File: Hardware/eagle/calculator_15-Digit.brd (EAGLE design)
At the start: 154.9 x 53.3 mm, 144 parts, among them M1 IRLML6402, M10 IRLML6401, M11 IRLML6401, M12 IRLML6402, M2 IRLML6402, M3 IRLML6401, M4 IRLML6401, M5 IRLML6401, M6 IRLML6401, M7 IRLML6401, M8 IRLML6401, M9 IRLML6401, U1 74HC4051_MUX, U2 TC1262-3.3VDB, U3 ATMEGA1284P-PU, U5 CON, X1 MICROMATCH-12, X3 MICROMATCH-12, Y2 12MHz

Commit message: New Hardware Design V0.4
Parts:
- removed BH1, BH2, BH3: BATTERY_HOLDER_AAAHOLDER_AAA, SparkFun-Electromechanical:BATTERY-AAA-KIT
- removed C12, C19: 15n, rcl:C025_050-025X075
- removed C17: 1n, rcl:C025_050-025X075
- removed C9: 2µ2, _jc:C025_050-025X075
- removed D29: SD103CW, BaseApp:SMADIODE
- removed JP3: DCF77, adafruit:1X01-CLEANBIG
- removed M12, M2: IRLML6402, IRLML6402:SOT-23
- removed R27, R45: 27k, rcl:0204/7
- removed R28: 6k8, rcl:0204/7
- removed R44: 47k, rcl:0204/7
- removed R46, R47, R53: 8k2, rcl:0204/7
- removed R52: 22, rcl:0204/7
- removed S2: RESET, _jc:B3F-10XX
- removed U2: TC1262-3.3VDB, parts:SOT223
- removed U5: CON, BaseApp:AUDIO-JACK
- added BH10, BH12, BH8: HOLDER_AAA_RIGHT, SparkFun-Electromechanical:BATTERY-AAA-RIGHT
- added BH11, BH7, BH9: HOLDER_AAA_LEFT1, SparkFun-Electromechanical:BATTERY-AAA-LEFT
- added C16: 0.1uF, SparkFun:0805
- added C20, C21: 10uF, SparkFun:EIA3216
- added C22: 15n, rcl:C1206K
- added D10, D7, D8, D9: SD103CW, BaseApp:SMADIODE
- added R2: 6k8, rcl:0204/5
- added R3: 27k, rcl:R1206
- added S3: B3F-4150, SmartPrj:TACTILE-PTH-12MM
- added U$1: IRLML6244, transistor-power:MICRO3
- added U4: TLV70033, SparkFun:SOT23-5
- C10: device rcl:C025_050-025X075 -> rcl:C1206K
- C11: value 15n -> 1n; device rcl:C025_050-025X075 -> SparkFun:0805
- C5: value 2µ2 -> 15n; device _jc:C025_050-025X075 -> rcl:C1206K
- JP13, JP14: value PINHD-2X7 -> (none); device pinhead:ZX07 -> pinhead:2X07
- M1: value IRLML6402 -> IRLML2244
- M10, M11, M3, M4, M5, M6, M7, M8, M9: value IRLML6401 -> IRLML2244
- R20: value 27k -> 2R7; device rcl:0204/7 -> rcl:0204/5
- R23: value 27k -> 6k8; device rcl:0204/7 -> rcl:R1206
- R24: value 6k8 -> 2R7; device rcl:0204/7 -> rcl:R1206
- R25: value 27k -> 100
- R26: value 6k8 -> 27k; device rcl:0204/7 -> rcl:0204/5
- R30: value 3k3 -> 3V3
- R31: value 68 -> 39
- R32: value 100 -> 39
- R35: value 8k2 -> 3k3
- R48: value 1k -> 3k3
- SG1: value BUZZERPTH-KIT -> BUZZERNS; device SparkFun-Electromechanical:BUZZER-12MM-KIT -> SparkFun-Electromechanical:BUZZER-12MM-NS
- U$2: value IRLML2502 -> IRLML6244
- moved C5 225.1 mm to (-68.6, -68.6), turned to 0 degrees
- moved R25 103.0 mm to (-66.0, -76.2)
- moved R23 85.3 mm to (-48.3, -45.7)
- moved R24 54.9 mm to (-48.3, -7.62)
- moved R20 42.1 mm to (-45.7, -15.2), turned to 0 degrees
- moved C10 40.5 mm to (-55.9, 15.2), turned to 180 degrees
- moved C11 40.3 mm to (-50.8, 15.2), turned to 180 degrees
- moved R26 35.3 mm to (-58.4, 7.62), turned to 180 degrees
- moved D6 34.5 mm to (-58.4, -48.3), turned to 180 degrees
- moved D1 24.0 mm to (-58.4, -55.9), turned to 180 degrees
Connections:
- net D11 renamed D5_
- net D12 renamed D6_
- net D13 renamed D7_
- net D14 renamed D0_
- net RXD_0 renamed D8_
- net TXD_0 renamed D9_
- removed net 3V5: C1.1, C2.1, C3.1, C6.1, D5.C, D6.C, JP5.2, R1.1, R21.1, R22.1, R4.1, U2.3, U3.10
- removed net A_0: KP1.C_2, KP2.C_2, R24.1
- removed net A_1: KP1.C_1, KP2.C_1, R26.1
- removed net A_2: KP1.C_0, KP2.C_0, R28.1
- removed net D4: C17.1, R35.1, U3.18
- removed net INH: R45.1, U$2.3, U1.6
- removed net N$24: C15.1, R31.1, R32.2
- removed net N$29: M3.1, R34.1, R48.2
- removed net N$8: C19.1, M12.1, M2.1, R45.2, R47.1
- removed net N$9: R46.1, R47.2, S2.1, S2.2
- removed net OFF: D29.A, R20.2, R44.1, U$2.1
- removed net SEG_C_SOURCE: JP10.1, M6.3
- removed net SEG_DP_SOURCE: JP7.1, M11.3
- removed net V_DCF77: C9.1, R52.2, R53.1, U5.TIP
- new net 3V3: C1.1, C16.1, C2.1, C20.A, C3.1, C6.1, D5.C, D6.C, D7.A, R1.1, R21.1, R22.1, R4.1, U3.10, U4.5
- new net A8: C22.1, R35.1, R48.2
- new net A9: C5.1, R25.1, R26.2, R3.2
- new net D12_: D9.A, D9.C, R48.1, U$1.2, U$1.3, U3.18
- new net EN: C10.1, C5.2, D10.C, R2.2, R23.2, R26.1, R3.1, U$2.1, U4.3
- new net GND1: C22.2
- new net IO: U$2.3, U1.3
- new net N$6: S3.P$13, S3.P$14, S3.P$23, S3.P$24, S3.P$3, S3.P$4
- new net XX4: C14.2, C15.2, R32.1, SG1.-
- new net XX_3: D8.A, R20.1, R24.1
- net A0: now also C15.1, R31.1; no longer R32.1
- net A4: now also R32.2
- net A5: now also KP1.C_0, KP2.C_0; no longer C12.1, R27.1, R28.2
- net A6: now also KP1.C_1, KP2.C_1; no longer C11.1, R25.1, R26.2
- net A7: now also KP1.C_2, KP2.C_2; no longer C10.1, R23.1, R24.2
- net AREF: no longer C5.1, R23.2, R25.2, R27.2
- net D18: now also D10.A, U$1.1; no longer D29.C
- net D7: no longer JP3.1, JP6.2, R53.2, U5.RING
- net GND: now also C16.2, C20.C, C21.C, JP6.2, R2.1, R23.1, S3.P$15, U1.6, U4.2; no longer BH1.M1, BH1.M2, C12.2, C14.2, C15.2, C5.2, C9.2, SG1.-, U1.3, U5.SLEEVE
- net GND_POWER: no longer R20.1, S2.3, S2.4, U$2.2, U2.2, U2.4
- net N$1: now also M3.1, R34.1; no longer C17.2, R48.1
- net N$2: now also U$2.2; no longer BH1.P1, BH1.P2, BH2.M1, BH2.M2
- net N$3: now also C11.1, U4.4; no longer BH2.P1, BH2.P2, BH3.M1, BH3.M2
- net N$7: now also D8.C; no longer M12.2, M2.2, R46.2
- net NC1: now also BH11.P1, BH11.P2, BH11.P3, BH11.P4, BH4.P3, BH4.P4, BH7.P1, BH7.P2, BH7.P3, BH7.P4, BH9.P1, BH9.P2, BH9.P3, BH9.P4
- net NC2: now also BH5.P3, BH5.P4
- net NC3: now also BH10.M1, BH10.M2, BH10.M3, BH10.M4, BH12.M1, BH12.M2, BH12.M3, BH12.M4, BH6.M3, BH6.M4, BH8.M1, BH8.M2, BH8.M3, BH8.M4
- net SEG_C: now also JP10.1, M6.3
- net SEG_DP: now also JP7.1, M11.3
- net VCC: now also JP5.2, R20.2, R24.2; no longer BH3.P1, BH3.P2, M2.3
- net V_IN: now also C21.A, D7.C, S3.P$1, S3.P$11, S3.P$12, S3.P$2, S3.P$21, S3.P$22, U4.1; no longer C19.2, M12.3, R44.2, R52.1, U2.1
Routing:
- net SEG_DP: track 327.7 -> 347.3 mm
- net SEG_DP_SOURCE: track 19.6 -> 0.00 mm
- net SEG_C_SOURCE: track 9.56 -> 0.00 mm
- net SEG_C: track 271.7 -> 281.2 mm

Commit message: New Hardware Design V0.4a
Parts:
- removed C13: 15n, rcl:C025_050-025X075
- removed D10, D9: SD103CW, BaseApp:SMADIODE
- removed S1: RESET, _jc:B3F-10XX
- removed U$1: IRLML6244, transistor-power:MICRO3
- removed X2, X4: (no value), pinhead:2X06
- added C12: 0.1uF, SparkFun:0805
- added C9: 1µ, rcl:C025_050-025X075
- added D11, D12: SD103CW, BaseApp:SMADIODE
- added M2: IRLML2244, IRLML6402:SOT-23
- added R27: 6k8, rcl:R1206
- added R28, R44: 47k, rcl:0204/7
- C18: value 15n -> 100n
- C4: value 2µ2 -> 1µ; device _jc:C025_050-025X075 -> rcl:C025_050-025X075
- R1: value 68k -> 47k
- R26, R3: value 27k -> 6k8
- R31, R32: value 39 -> 100
- moved C5 94.4 mm to (-30.5, 17.8)
- moved R25 94.4 mm to (-27.9, 10.2)
- moved C4 55.7 mm to (-30.5, 5.08)
- moved U3 50.6 mm to (53.3, 1.27), turned to 270 degrees
- moved C10 40.2 mm to (-33.0, -17.8), turned to 0 degrees
- moved D8 36.6 mm to (-66.0, -30.5)
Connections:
- net D8 renamed D2_
- net SCL renamed D16_
- net SDA renamed D17_
- removed net 3V3: C1.1, C16.1, C2.1, C20.A, C3.1, C6.1, D5.C, D6.C, D7.A, R1.1, R21.1, R22.1, R4.1, U3.10, U4.5
- removed net D10: JP13.9, U3.5, X2.7
- removed net D15: U3.2
- removed net D18: D10.A, U$1.1, U3.24
- removed net D19: JP14.7, U3.25, X4.7
- removed net D2: JP1.1, U3.16
- removed net D20: JP14.6, U3.26, X4.6
- removed net D21: JP14.5, U3.27, X4.5
- removed net D22: JP14.4, U3.28, X4.4
- removed net D23: JP14.3, U3.29, X4.3
- removed net D3: JP2.1, U3.17
- removed net D5: JP13.8, U3.19, X2.6
- removed net D6: JP13.7, U3.20, X2.5
- removed net D7: U3.21
- removed net D9: U3.4
- removed net IO: U$2.3, U1.3
- removed net IO_A__: JP13.11, X2.9
- removed net IO_B__: JP13.12, X2.10
- removed net IO_C__: JP13.13, X2.11
- removed net IO_D__: JP13.14, X2.12
- removed net N$7: D8.C
- removed net XX4: C14.2, C15.2, R32.1, SG1.-
- new net CA_PWM1: D12.A, M2.3
- new net D10_: JP1.1, JP13.10, U3.16
- new net D11_: JP13.8, JP2.1, U3.17
- new net D13_: JP13.7, U3.19
- new net D14_: JP14.1, U3.20
- new net D15_: JP14.2, U3.21
- new net D18_: R44.2, U3.24
- new net D19_: JP14.3, U3.25
- new net D1_: JP13.14, U3.2
- new net D20_: JP14.4, U3.26
- new net D21_: JP14.5, U3.27
- new net D22_: JP14.6, U3.28
- new net D23_: JP14.7, U3.29
- new net D3_: JP13.11, U3.4
- new net D4_: U3.5
- new net EN_: D11.C, D12.C, R27.1
- new net GND-ISO: C1.2, C12.2, C14.2, C15.2, C2.2, C3.2, C4.2, C6.2, C7.2, C8.2, D4.C, D5.A, JP5.6, JP6.1, JP6.2, U$2.3, U1.3, U1.6, U1.7, U1.8, U3.11, U3.31
- new net N$10: C15.1, C9.2, R32.1, SG1.-
- new net N$8: M2.1, R28.2, R44.1
- net /RESET: no longer S1.1, S1.2
- net A0: no longer C15.1
- net A5: now also KP1.C_2, KP2.C_2; no longer KP1.C_0, KP2.C_0
- net A7: now also KP1.C_0, KP2.C_0; no longer KP1.C_2, KP2.C_2
- net AREF: now also C12.1; no longer C13.1
- net CA_PWM: no longer X4.8
- net D0_: now also JP13.13
- net D12_: no longer D9.A, D9.C, U$1.2, U$1.3
- net D5_: no longer JP13.10, X2.8
- net D6_: now also JP13.12; no longer JP14.1, X4.1
- net D7_: now also JP13.9; no longer JP14.2, X4.2
- net EN: now also R27.2; no longer D10.C
- net GND: no longer C1.2, C13.2, C2.2, C3.2, C4.2, C6.2, C7.2, C8.2, D4.C, D5.A, JP5.6, JP6.1, JP6.2, S1.3, S1.4, U1.6, U1.7, U1.8, U3.11, U3.31
- net IO_A: no longer X2.4
- net IO_B: no longer X2.3
- net IO_C: no longer X2.2
- net IO_D: no longer X2.1
- net IO_DP: no longer X4.9
- net IO_E: no longer X4.12
- net IO_F: no longer X4.11
- net IO_G: no longer X4.10
- net N$23: now also C9.1
- net VCC: now also C1.1, C16.1, C2.1, C20.A, C3.1, C6.1, D5.C, D6.C, D7.A, D8.C, M2.2, R1.1, R21.1, R22.1, R28.1, R4.1, U3.10, U4.5
- net XX_3: now also D11.A

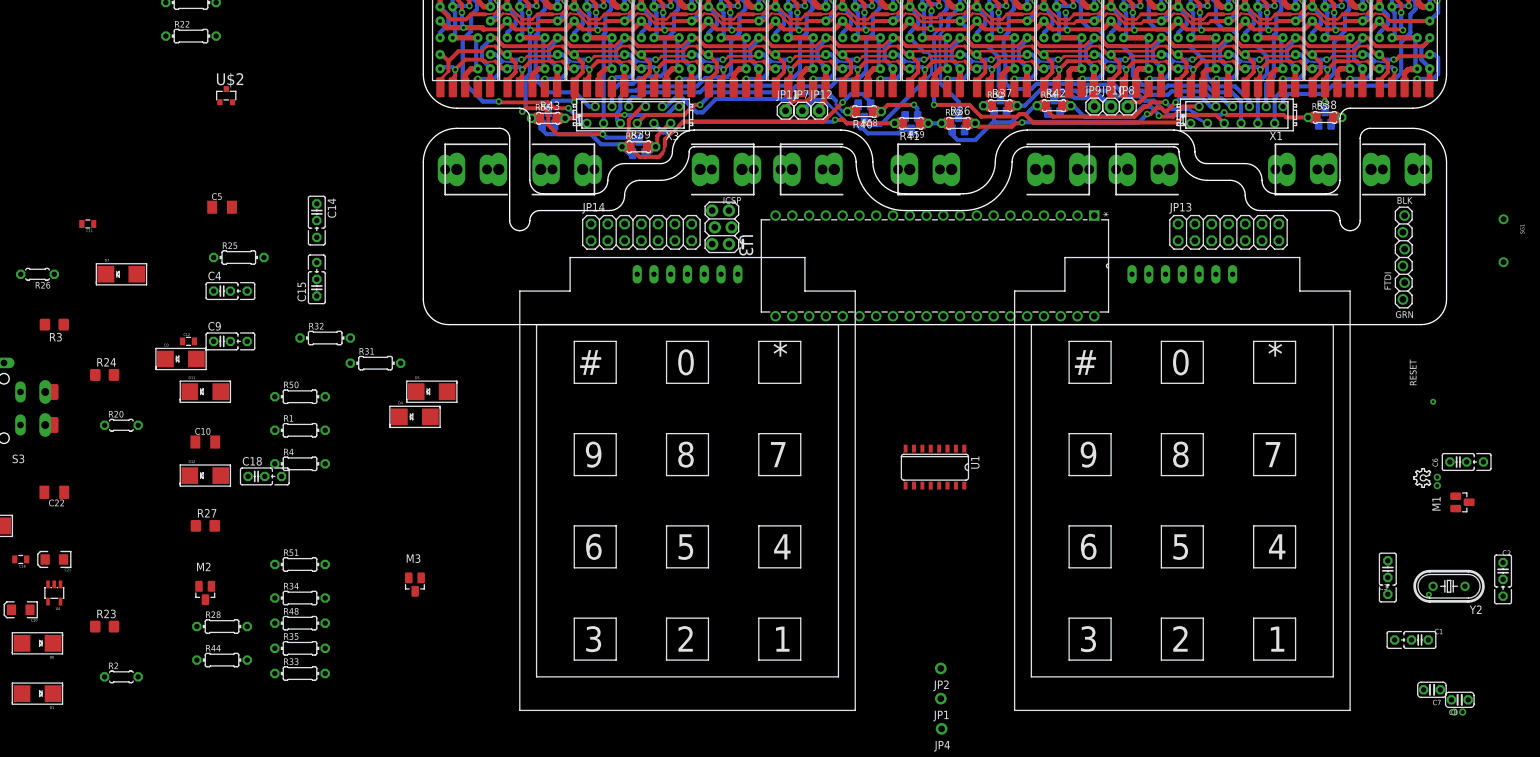
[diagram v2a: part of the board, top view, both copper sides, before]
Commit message: Display .. 5x LTD040AUE-101A 3-digit_Display
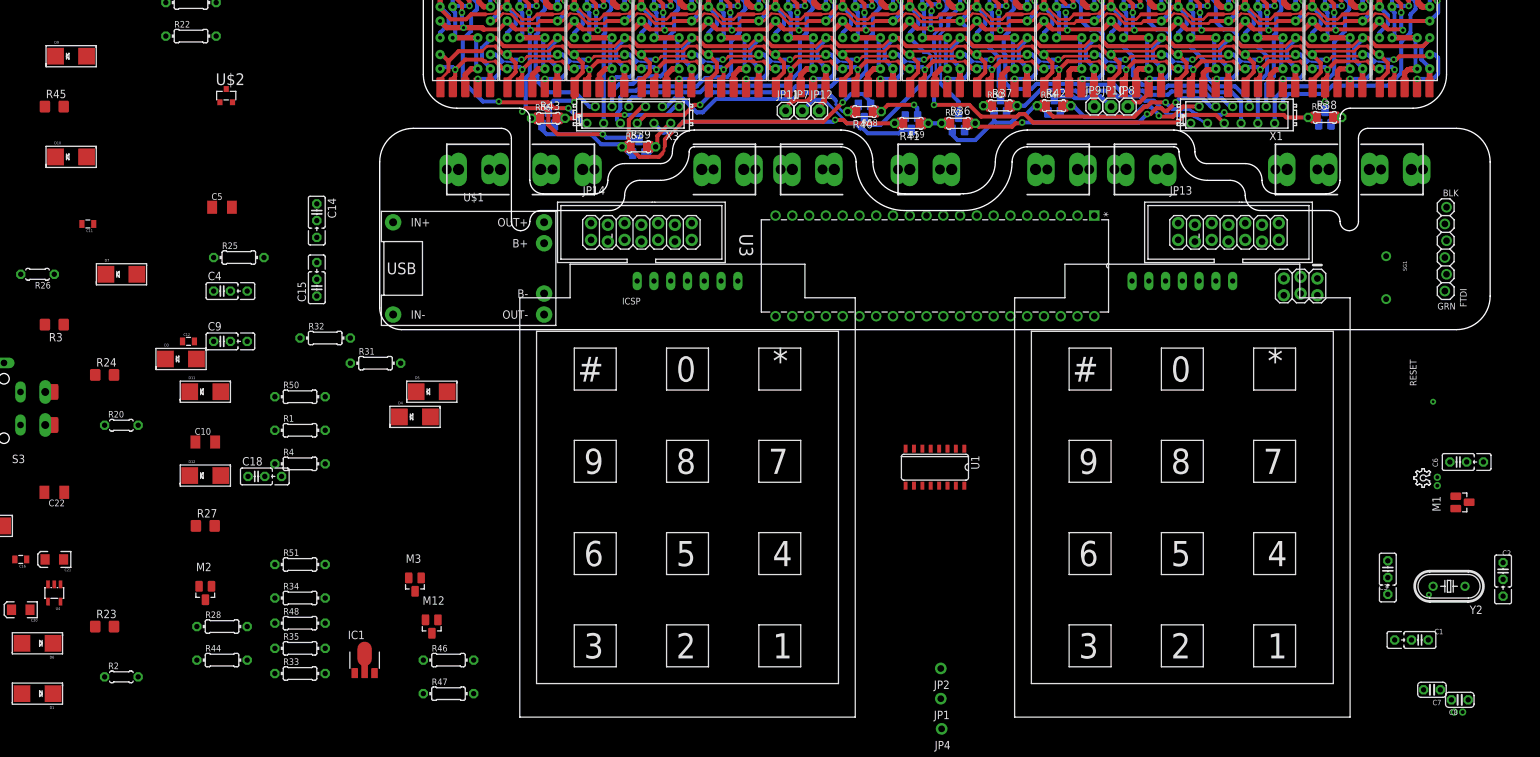
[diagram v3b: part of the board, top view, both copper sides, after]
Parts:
- added D10, D9: SD103CW, BaseApp:SMADIODE
- added IC1: MCP170333MB, linear:SOT89
- added M12: IRLML2244, IRLML6402:SOT-23
- added R45: 56R, rcl:R1206
- added R46, R47: 47k, rcl:0204/7
- added U$1: BATTERY-CHARGER-LI-PROT, diy-modules:BATTERY-CHARGER-LI-PROT
- added U$3: HT7333, HT7333_SOT89:SOT89
- C5: value 15n -> 100n
- moved JP5 89.0 mm to (135.4, 7.11), turned to 180 degrees
- moved SG1 18.6 mm to (145.8, 7.11)
- moved JP6 6.48 mm to (154.9, 17.8)
- moved KP1 1.02 mm to (40.0, 6.60)
- moved KP2 1.02 mm to (114.9, 6.60)
- moved BH9 0.25 mm to (109.0, 23.5)
- moved BH8 0.25 mm to (7.87, 23.5)
- moved BH10 0.25 mm to (46.0, 23.5)
- moved BH7 0.25 mm to (147.1, 23.5)
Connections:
- new net B_MINUS: BH8.M1, BH8.M2, BH8.M3, BH8.M4, U$1.B-
- new net CA_PWM2: D11.A, M12.3
- new net N$13: R45.2, U$1.IN+
- new net N$9: M12.1, R46.2, R47.1
- new net P2: BH10.M1, BH10.M2, BH10.M3, BH10.M4, BH12.M1, BH12.M2, BH12.M3, BH12.M4
- new net P3: BH11.P1, BH11.P2, BH11.P3, BH11.P4, BH9.P1, BH9.P2, BH9.P3, BH9.P4
- new net VIN_P: D10.A, D9.A, R45.1, R47.2
- net GND: now also IC1.1, U$1.IN-, U$1.OUT-, U$3.GND
- net NC1: no longer BH11.P1, BH11.P2, BH11.P3, BH11.P4, BH9.P1, BH9.P2, BH9.P3, BH9.P4
- net NC3: no longer BH10.M1, BH10.M2, BH10.M3, BH10.M4, BH12.M1, BH12.M2, BH12.M3, BH12.M4, BH8.M1, BH8.M2, BH8.M3, BH8.M4
- net VCC: now also IC1.3, R50.2, U$3.VOUT
- net V_IN: now also D9.C, IC1.2@1, U$1.B+, U$1.OUT+
- net XX_3: now also D10.C, M12.2, R46.1; no longer D11.A
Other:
- board size 154.9 x 53.3 mm -> 168.1 x 54.1 mm
